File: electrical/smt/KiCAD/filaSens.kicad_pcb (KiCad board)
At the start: 2 copper layers, 50 x 20 mm, 16 parts, among them IC2 SS495, IC3 TINY85

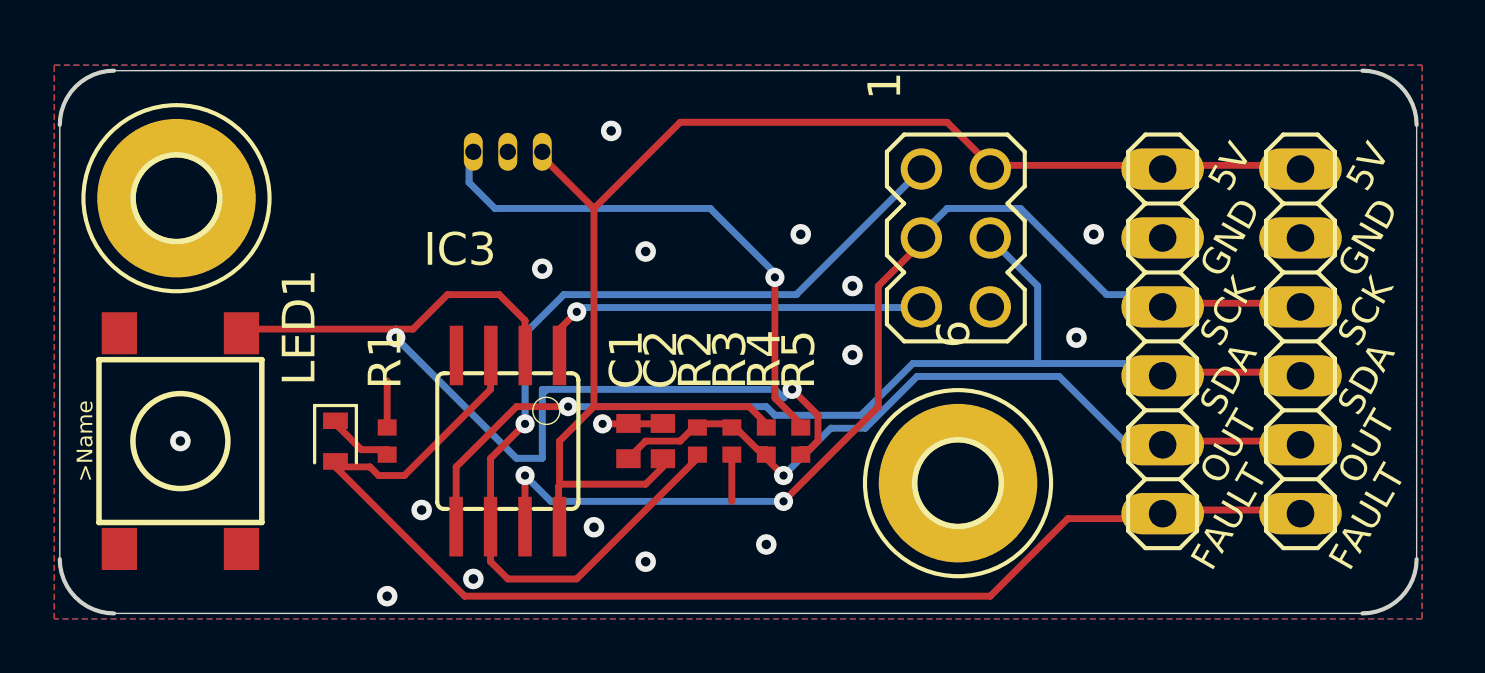
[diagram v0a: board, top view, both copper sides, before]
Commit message: fix capacitor grounds not connected
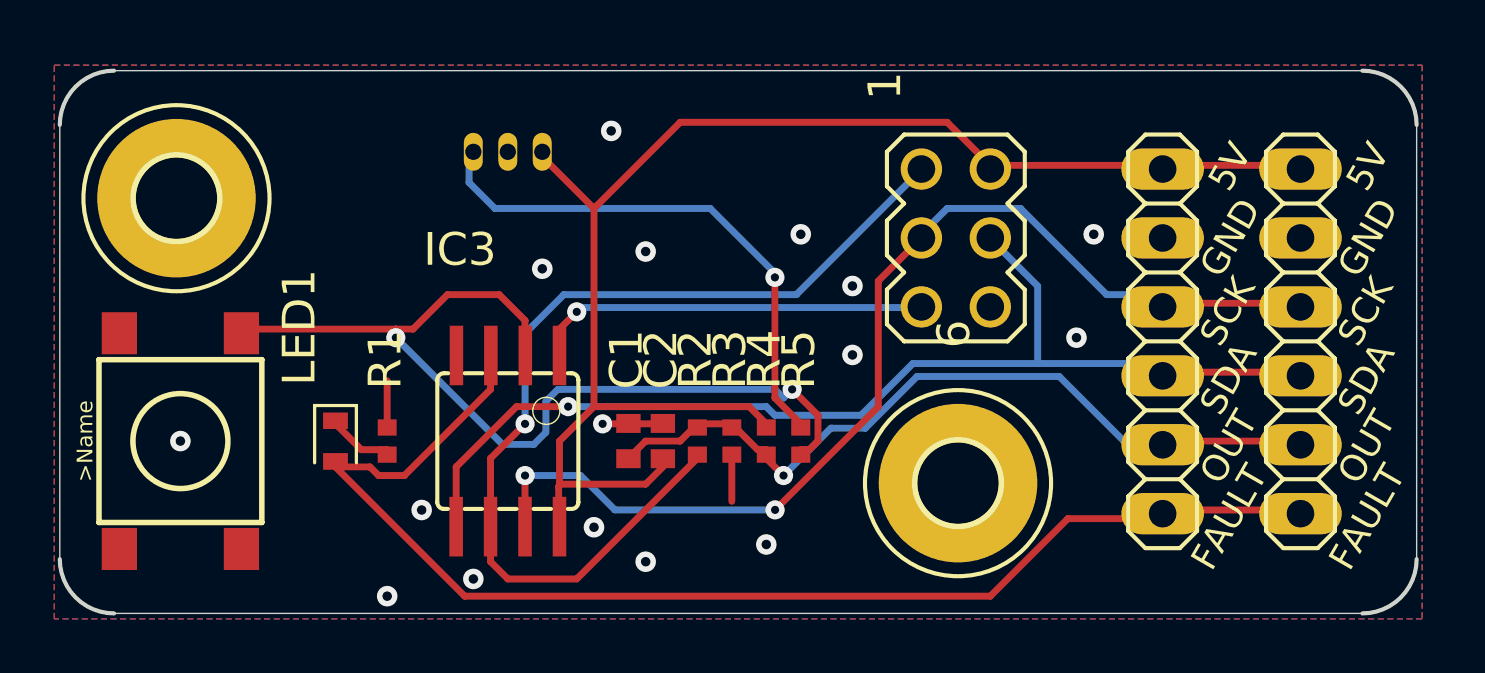
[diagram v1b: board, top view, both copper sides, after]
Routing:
- net /IN: track 35.7 -> 34.3 mm
